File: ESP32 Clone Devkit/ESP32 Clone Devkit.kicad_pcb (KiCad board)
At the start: 4 copper layers, 0 parts

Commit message: Define pcb outline size and shape
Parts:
- added C1: 22uF/10V(20%), Capacitor_SMD:C_0201_0603Metric, F.Cu at (234.4, 131.6)
- added C2: 22uF/10V(20%), Capacitor_SMD:C_0201_0603Metric, F.Cu at (234.4, 133.4)
- added C3: 4.7uF/6.3V(20%), Capacitor_SMD:C_01005_0402Metric, F.Cu at (225.3, 131.6)
- added C4: 0.1uF/50V(10%), Capacitor_SMD:C_01005_0402Metric, F.Cu at (225.3, 133.2)
- added C5: 22uF/10V(20%), Capacitor_SMD:C_0201_0603Metric, F.Cu at (234.4, 135.1)
- added C6: 0.1uF/50V(10%), Capacitor_SMD:C_01005_0402Metric, F.Cu at (225.3, 134.9)
- added C7: 0.1uF/50V(10%), Capacitor_SMD:C_01005_0402Metric, F.Cu at (225.3, 136.5)
- added C8: 0.1uF/50V(10%)(NC), Capacitor_SMD:C_01005_0402Metric, F.Cu at (227.6, 131.6)
- added C9: 0.1uF/50V(10%), Capacitor_SMD:C_01005_0402Metric, F.Cu at (227.6, 133.2)
- added D1: LED, LED_SMD:LED_0603_1608Metric, F.Cu at (237.7, 135.0)
- added D2: D_Schottky, Diode_SMD:D_SOD-323, F.Cu at (237.8, 132.2)
- added D3: D_TVS, Diode_SMD:D_SOD-523, F.Cu at (237.5, 124.2)
- added D4: D_TVS, Diode_SMD:D_SOD-523, F.Cu at (237.5, 126.6)
- added D5: D_TVS, Diode_SMD:D_SOD-523, F.Cu at (237.5, 129.1)
- added J1: USB_B_Micro, Connector_USB:USB_Micro-AB_Molex_47590-0001, F.Cu at (229.9, 127.6)
- added J2: Conn_01x19_Pin, Connector_PinHeader_2.54mm:PinHeader_1x19_P2.54mm_Vertical, F.Cu at (62.8, 65.4)
- added J3: Conn_01x19_Pin, Connector_PinHeader_2.54mm:PinHeader_1x19_P2.54mm_Vertical, F.Cu at (89.7, 65.4)
- added MOD1: ESP32-WROOM-32, digikey-footprints:ESP32-WROOM-32D, F.Cu at (76.3, 72.4)
- added Q1: MMSS8050-H-TP, digikey-footprints:SOT-23-3, F.Cu at (215.5, 134.1)
- added Q2: MMSS8050-H-TP, digikey-footprints:SOT-23-3, F.Cu at (220.2, 134.1)
- added R1: 2k(5%), Resistor_SMD:R_01005_0402Metric, F.Cu at (227.6, 134.9)
- added R10: 10k(5%), Resistor_SMD:R_01005_0402Metric, F.Cu at (232.1, 136.5)
- added R2: 10k(5%), Resistor_SMD:R_01005_0402Metric, F.Cu at (227.6, 136.5)
- added R3: 10k(5%), Resistor_SMD:R_01005_0402Metric, F.Cu at (229.8, 131.6)
- added R4: 0R(5%), Resistor_SMD:R_01005_0402Metric, F.Cu at (229.8, 133.2)
- added R5: 0R(5%), Resistor_SMD:R_01005_0402Metric, F.Cu at (229.8, 134.9)
- added R6: 2k(5%), Resistor_SMD:R_01005_0402Metric, F.Cu at (229.8, 136.5)
- added R7: 47.5k(5%), Resistor_SMD:R_01005_0402Metric, F.Cu at (232.1, 131.6)
- added R8: 22.1k(5%), Resistor_SMD:R_01005_0402Metric, F.Cu at (232.1, 133.2)
- added R9: 10k(5%)(NC), Resistor_SMD:R_01005_0402Metric, F.Cu at (232.1, 134.9)
- added SW1: SW_Push, Button_Switch_SMD:SW_SPST_B3S-1000, F.Cu at (218.7, 118.9)
- added SW2: SW_Push, Button_Switch_SMD:SW_SPST_B3S-1000, F.Cu at (218.7, 127.4)
- added U1: CP2102N-A02-GQFN28, Package_DFN_QFN:TQFN-28-1EP_5x5mm_P0.5mm_EP2.7x2.7mm, F.Cu at (237.4, 90.7)
- added U2: AMS1117-3.3, Package_TO_SOT_SMD:SOT-223-3_TabPin2, F.Cu at (229.1, 118.8)
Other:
- board outline added: 30.9 x 56.9 mm

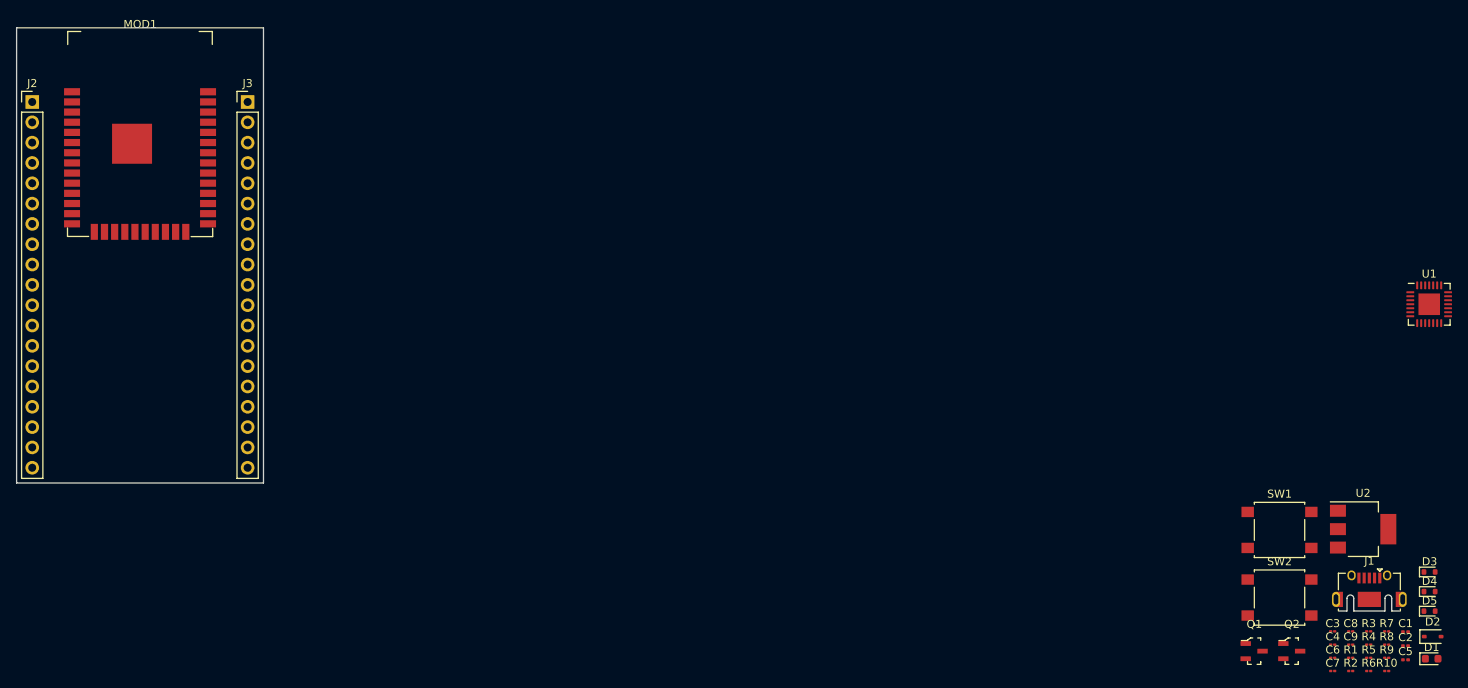
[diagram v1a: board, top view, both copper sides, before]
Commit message: place components
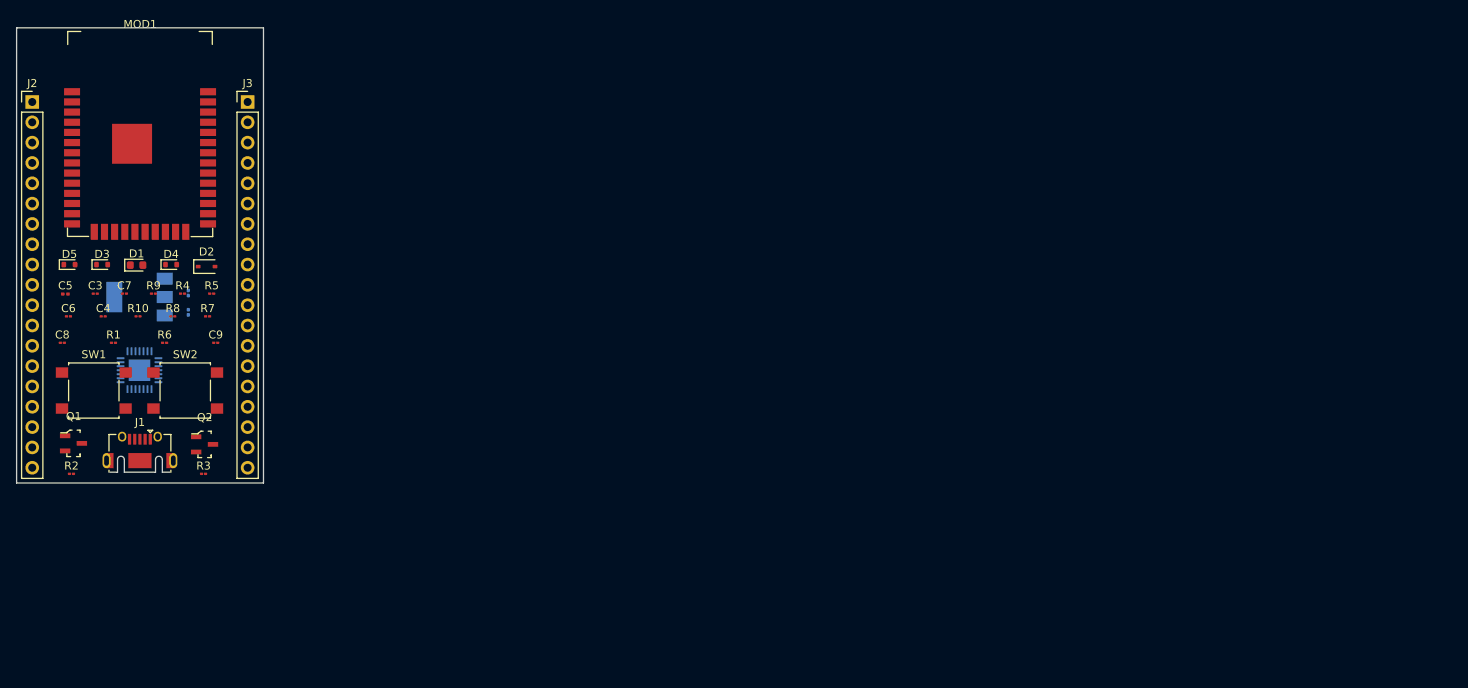
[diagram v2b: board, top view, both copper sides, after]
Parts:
- C1, C2, U1, U2: moved to B.Cu
- moved D5 175.4 mm to (67.4, 85.7)
- moved C5 173.6 mm to (66.9, 89.4)
- moved D3 170.3 mm to (71.5, 85.7)
- moved D1 169.2 mm to (75.8, 85.8)
- moved C8 165.0 mm to (66.5, 95.5)
- moved C6 163.7 mm to (67.3, 92.2)
- moved D4 162.5 mm to (80.1, 85.7)
- moved R10 162.3 mm to (76.0, 92.2)
- moved R2 161.8 mm to (67.7, 111.9)
- moved U1 161.4 mm to (76.2, 98.9), turned to 180 degrees
- moved R9 160.7 mm to (77.9, 89.4)
- moved C3 160.3 mm to (70.7, 89.4)
- moved D2 160.1 mm to (84.6, 86.0)
- moved R1 159.6 mm to (72.9, 95.5)
- moved C4 159.1 mm to (71.7, 92.2)
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
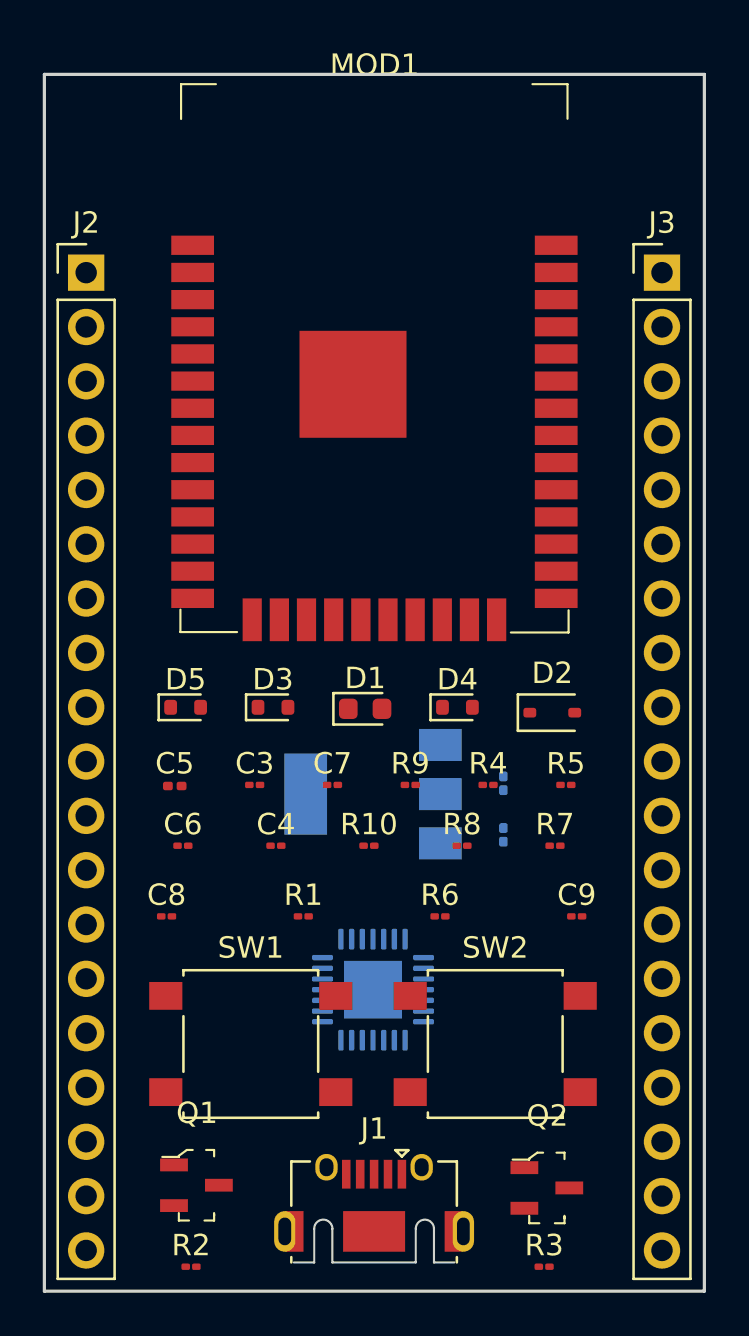
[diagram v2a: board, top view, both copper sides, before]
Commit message: refine outline
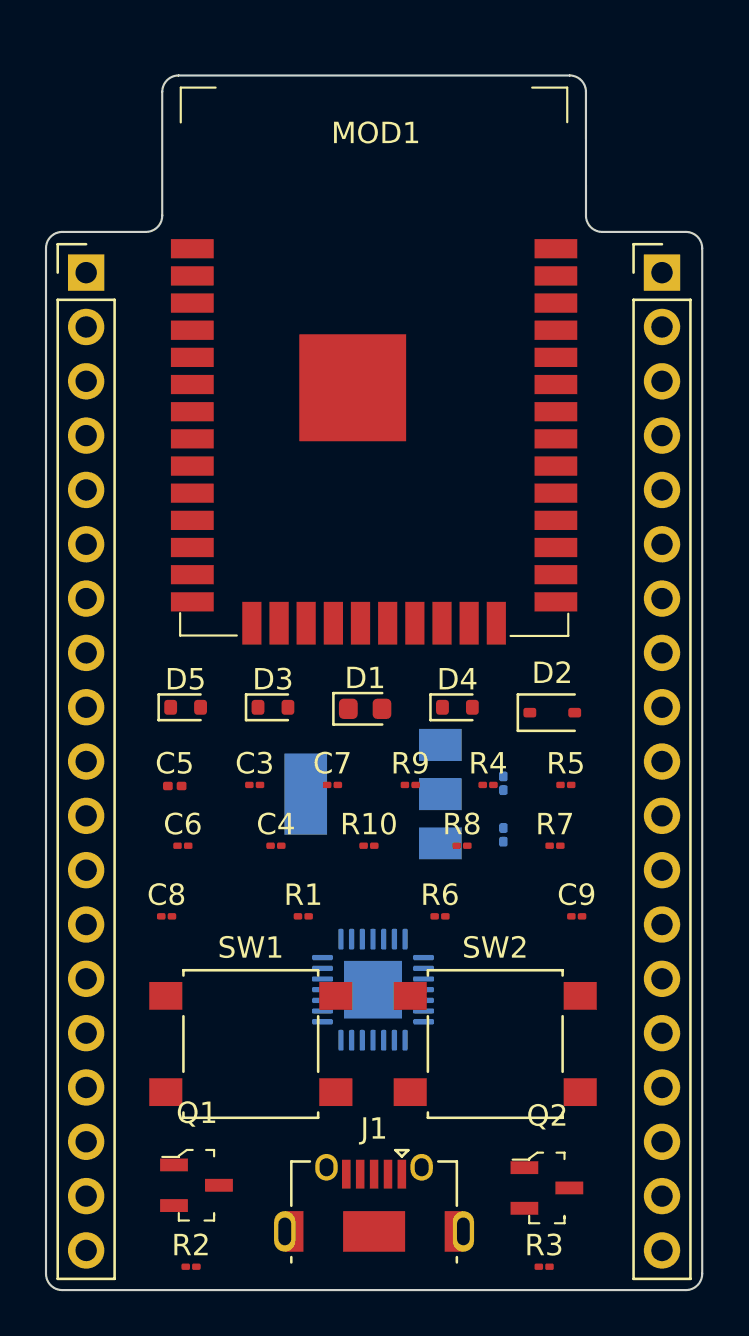
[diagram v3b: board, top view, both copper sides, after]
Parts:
- moved MOD1 0.16 mm to (76.3, 72.5)
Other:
- board size 30.9 x 56.9 mm -> 30.7 x 56.8 mm

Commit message: add new project
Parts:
- moved C2 2.31 mm to (82.6, 89.4)
- moved C1 2.04 mm to (82.7, 91.3)
- moved R8 0.94 mm to (81.1, 91.6)
- moved R1 0.79 mm to (73.7, 95.4)
- moved R2 0.70 mm to (67.8, 111.2), turned to 180 degrees
- moved C8 0.18 mm to (66.7, 95.4), turned to 180 degrees
- turned C3 to 180 degrees
- turned R5 to 180 degrees
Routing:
- net GND: track 0.00 -> 163.1 mm, vias 0 -> 5
- net /EN: track 0.00 -> 82.0 mm, vias 0 -> 8
- net /VDD33: track 0.00 -> 78.5 mm, vias 0 -> 5
- net /IO0: track 0.00 -> 64.1 mm, vias 0 -> 3
- net /DTR: track 0.00 -> 46.5 mm, vias 0 -> 2
- net /EXT_5V: track 0.00 -> 43.1 mm, vias 0 -> 4
- net /RTS: track 0.00 -> 42.2 mm, vias 0 -> 1
- net /VBUS: track 0.00 -> 39.8 mm, vias 0 -> 4
- net /CLK: track 0.00 -> 39.7 mm
- net /CMD: track 0.00 -> 36.8 mm
- net /USB_DN: track 0.00 -> 36.4 mm, vias 0 -> 3
- net /SD0: track 0.00 -> 36.0 mm
- net /SD3: track 0.00 -> 33.7 mm
- net /SD1: track 0.00 -> 32.3 mm
- net /SD2: track 0.00 -> 29.9 mm
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- added copper zone on F.Cu, net /VDD33
- added copper zone on B.Cu, net GND
